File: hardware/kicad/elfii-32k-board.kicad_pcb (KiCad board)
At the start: 2 copper layers, 177.8 x 127.1 mm, 15 parts, among them J1 ELFII_86_MECH_UNVERIFIED, U1 74HCT273, U2 62256, U3 74HCT04, U4 74HCT86, U5 74HCT32

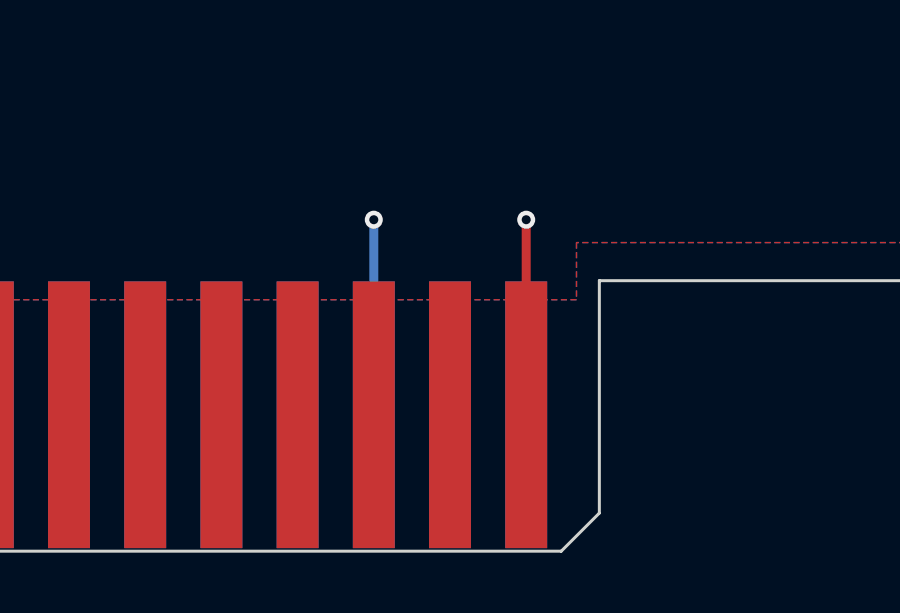
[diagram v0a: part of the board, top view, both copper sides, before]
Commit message: Restore last KiCad-loadable routed PCB checkpoint; defer unverified split power-plane experiment
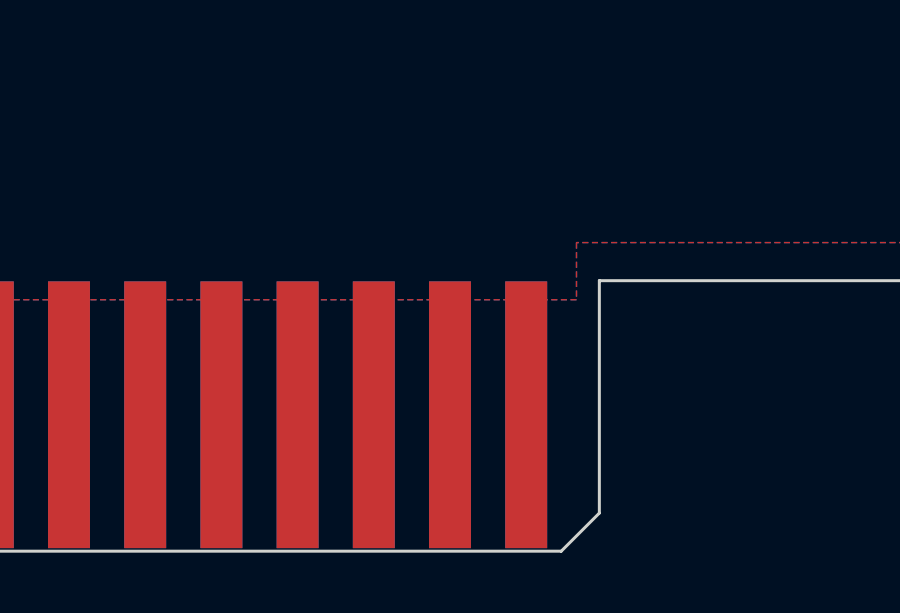
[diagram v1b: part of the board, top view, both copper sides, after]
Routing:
- net /VCC: track 6.50 -> 0.00 mm, vias 1 -> 0
- net /GND: track 6.50 -> 0.00 mm, vias 1 -> 0
- added copper zone on B.Cu, net /GND
- removed copper zone on B.Cu, net /VCC
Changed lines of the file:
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@@
   (via (at 122.555 139.827) (size 0.6) (drill 0.3) (layers "F.Cu" "B.Cu") (net 24))
   (via (at 97.155 143.002) (size 0.6) (drill 0.3) (layers "F.Cu" "B.Cu") (net 24))
-(segment (start 173.5836 148.7424) (end 173.5836 142.24) (width 0.3) (layer "F.Cu") (net 37))
-(via (at 173.5836 142.24) (size 0.6) (drill 0.3) (layers "F.Cu" "B.Cu") (net 37))
-(segment (start 168.5036 148.7424) (end 168.5036 142.24) (width 0.3) (layer "B.Cu") (net 18))
-(via (at 168.5036 142.24) (size 0.6) (drill 0.3) (layers "F.Cu" "B.Cu") (net 18))
 (zone (net 18) (net_name "/GND") (layer "F.Cu")
 (hatch edge 0.508)
@@
 (polygon (pts (xy 33.02 27.94) (xy 206.375 27.94) (xy 206.375 143.002) (xy 175.26 143.002) (xy 175.26 144.907) (xy 65.278 144.907) (xy 65.278 143.002) (xy 33.02 143.002)))
 )
-(zone (net 37) (net_name "/VCC") (layer "B.Cu")
+(zone (net 18) (net_name "/GND") (layer "B.Cu")
 (hatch edge 0.508)
 (connect_pads full (clearance 0.3))

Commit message: Implement front GND/back +5V planes and edge-finger power-via straps
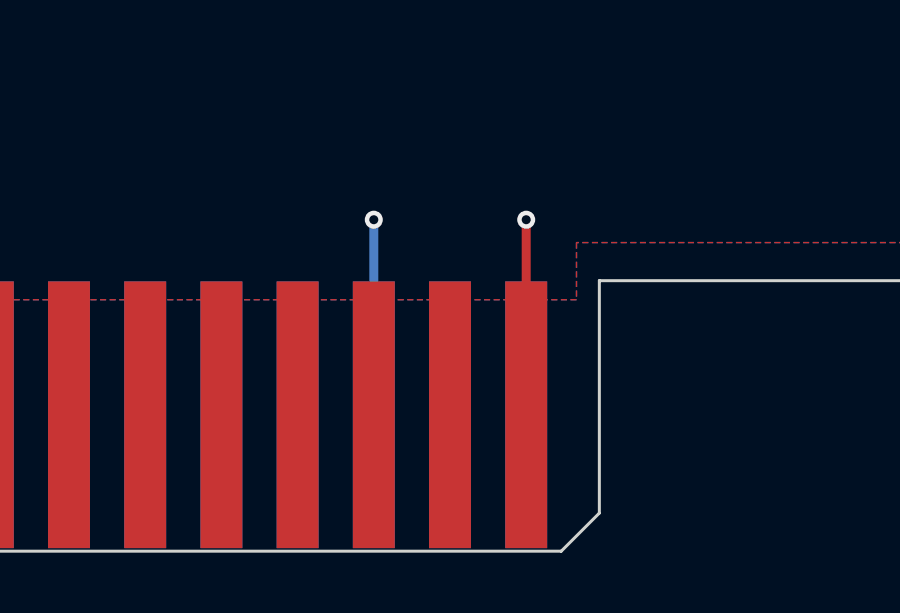
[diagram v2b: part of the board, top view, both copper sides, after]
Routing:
- net /VCC: track 0.00 -> 6.50 mm, vias 0 -> 1
- net /GND: track 0.00 -> 6.50 mm, vias 0 -> 1
- added copper zone on B.Cu, net /VCC
- removed copper zone on B.Cu, net /GND
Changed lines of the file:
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@@
 (polygon (pts (xy 33.02 27.94) (xy 206.375 27.94) (xy 206.375 143.002) (xy 175.26 143.002) (xy 175.26 144.907) (xy 65.278 144.907) (xy 65.278 143.002) (xy 33.02 143.002)))
 )
-(zone (net 18) (net_name "/GND") (layer "B.Cu")
+(zone (net 37) (net_name "/VCC") (layer "B.Cu")
 (hatch edge 0.508)
 (connect_pads full (clearance 0.3))
@@
 (polygon (pts (xy 33.02 27.94) (xy 206.375 27.94) (xy 206.375 143.002) (xy 175.26 143.002) (xy 175.26 144.907) (xy 65.278 144.907) (xy 65.278 143.002) (xy 33.02 143.002)))
 )
+(segment (start 173.5836 148.7424) (end 173.5836 142.24) (width 0.3) (layer "F.Cu") (net 37))
+(via (at 173.5836 142.24) (size 0.6) (drill 0.3) (layers "F.Cu" "B.Cu") (net 37))
+(segment (start 168.5036 148.7424) (end 168.5036 142.24) (width 0.3) (layer "B.Cu") (net 18))
+(via (at 168.5036 142.24) (size 0.6) (drill 0.3) (layers "F.Cu" "B.Cu") (net 18))
 )
